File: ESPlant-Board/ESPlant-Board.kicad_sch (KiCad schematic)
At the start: 38 parts, among them J1 Conn_01x05, U1 HC-TYPE-C-16P-01A-G, U13 ESP32-C6-MINI-1/U, U3 AHT20-F, U4 Button, U6 Light sensor, U7 AMS1117-3_3, U8 MK-12C02-G025

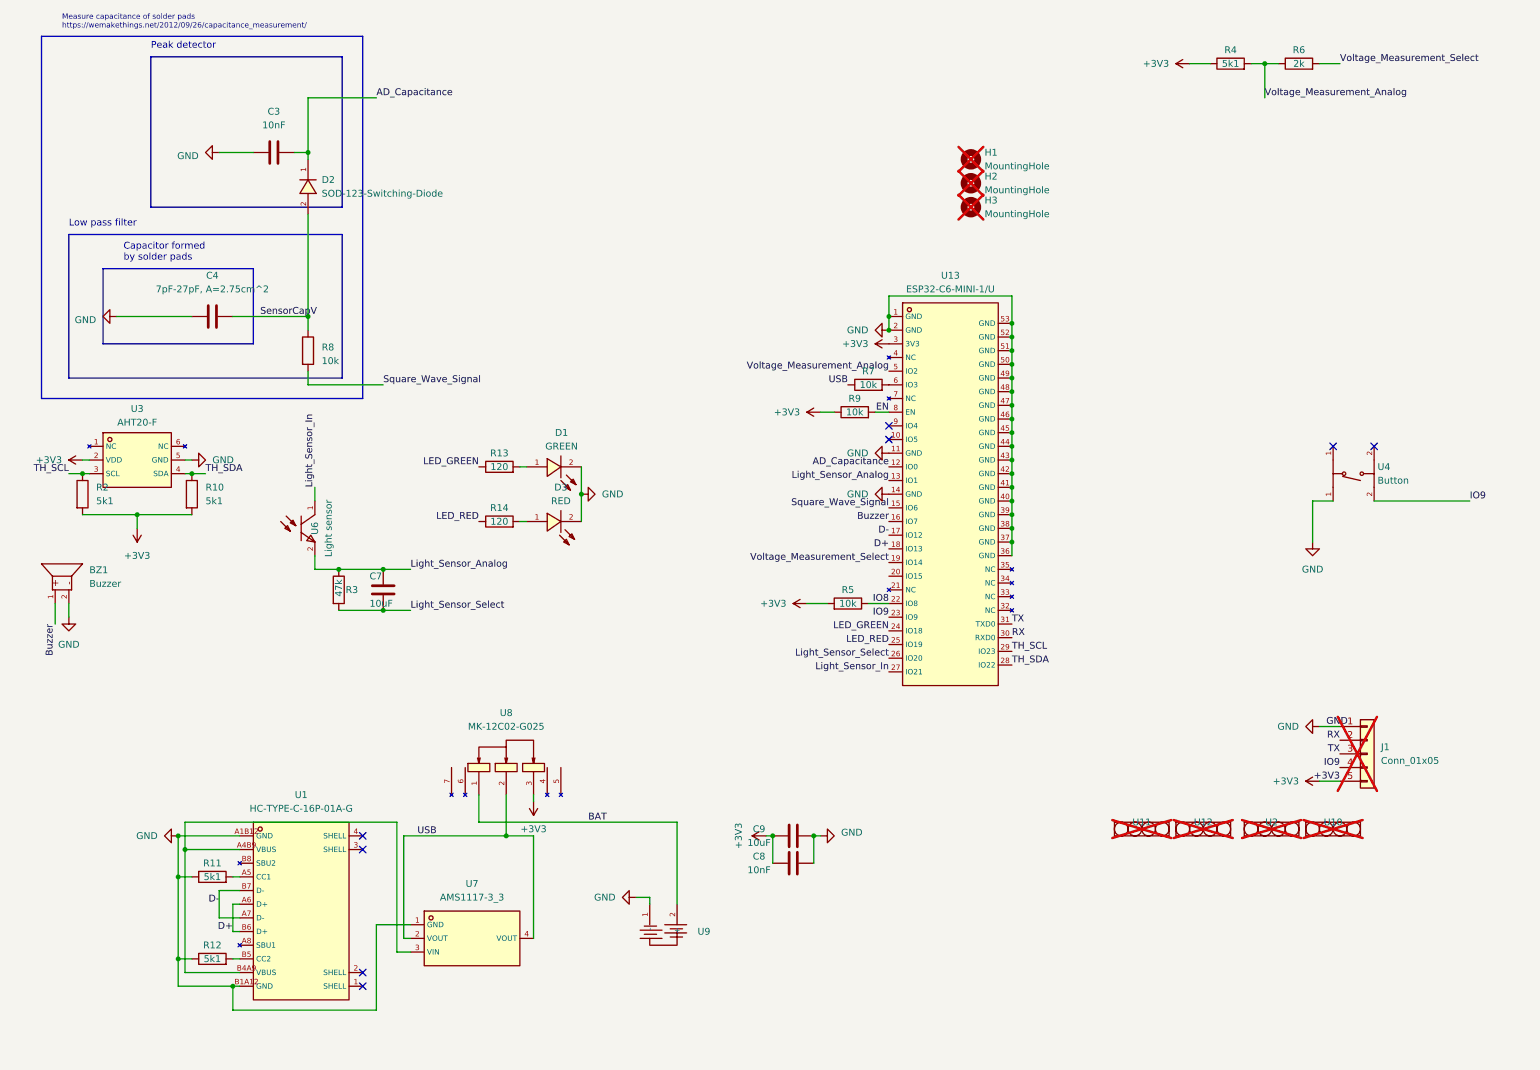
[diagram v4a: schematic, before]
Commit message: Board: New power supply chip
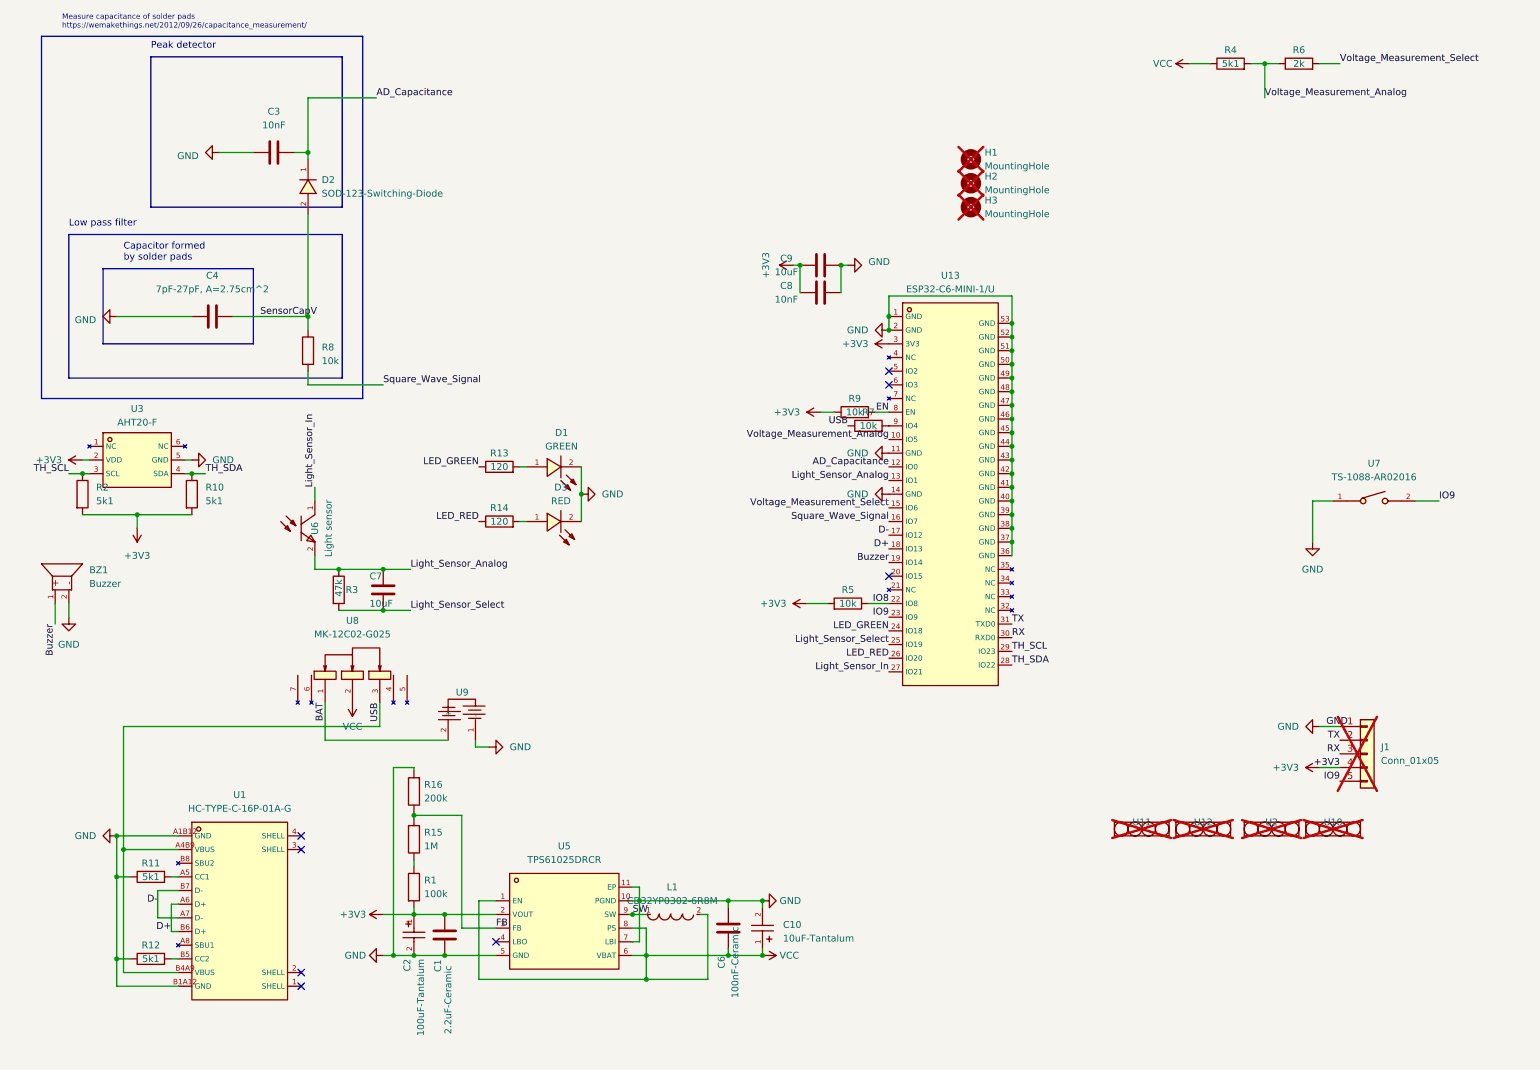
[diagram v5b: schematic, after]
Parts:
- removed U4: Button, CustomFootprints:SW-SMD_4P-L5.1-W5.1-P3.70-LS6.5-TL-2, symbol Custom_Parts:Button
- removed U7: AMS1117-3_3, CustomFootprints:SOT-223-3_L6.5-W3.4-P2.30-LS7.0-BR, symbol Custom_Parts:AMS1117_Voltage_Regulator
- added C1: 2.2uF-Ceramic, Capacitor_SMD:C_0402_1005Metric, symbol Device:C
- added C10: 10uF-Tantalum, CustomFootprints:CAP-SMD_L3.2-W1.6-RD-C7171, symbol Custom_Parts:TAJA106K016RNJ
- added C2: 100uF-Tantalum, CustomFootprints:CASE-B_3528, symbol Custom_Parts:TAJB107K006RNJ
- added C6: 100nF-Ceramic, Capacitor_SMD:C_0402_1005Metric, symbol Device:C
- added L1: CD32YP0302-6R8M, CustomFootprints:IND-SMD_L3.5-W3.0, symbol Custom_Parts:CD32YP0302-6R8M
- added R1: 100k, Resistor_SMD:R_0402_1005Metric, symbol Device:R
- added R15: 1M, Resistor_SMD:R_0402_1005Metric, symbol Device:R
- added R16: 200k, Resistor_SMD:R_0402_1005Metric, symbol Device:R
- added U5: TPS61025DRCR, CustomFootprints:VSON-10_L3.0-W3.0-P0.50-BL-EP_TPS62410DRCR, symbol Custom_Parts:TPS61025DRCR
- added U7: TS-1088-AR02016, CustomFootprints:SW-SMD_L3.9-W3.0-P4.45, symbol Custom_Parts:TS-1088-AR02016
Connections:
- net +3V3: now also J1.4 (Pin_4), C1.2, C2.1, R1.2, U5.2 (VOUT); no longer J1.5 (Pin_5), R4.1, U8.3
- net Buzzer: now also U13.19 (IO14); no longer U13.16 (IO7)
- net GND: now also C1.1, C10.2, C2.2, C6.2, R16.2, U5.10 (PGND), U5.11 (EP), U5.5 (GND), U5.7 (LBI), U7.1
- net IO9: now also J1.5 (Pin_5), U7.2; no longer J1.4 (Pin_4)
- net LED_RED: now also U13.26 (IO20); no longer U13.25 (IO19)
- net Light_Sensor_Select: now also U13.25 (IO19); no longer U13.26 (IO20)
- net RX: now also J1.3 (Pin_3); no longer J1.2 (Pin_2)
- net Square_Wave_Signal: now also U13.16 (IO7); no longer U13.15 (IO6)
- net TX: now also J1.2 (Pin_2); no longer J1.3 (Pin_3)
- net USB: now also U1.A4B9 (VBUS), U1.B4A9 (VBUS), U8.3; no longer U8.2
- net Voltage_Measurement_Analog: now also U13.10 (IO5); no longer U13.5 (IO2)
- net Voltage_Measurement_Select: now also U13.15 (IO6); no longer U13.19 (IO14)
- net at U13.6 (IO3): no longer R7.2
- net at U13.9 (IO4): now also R7.2
- new net: R1.1, R15.1
- new net FB: R15.2, R16.1, U5.3 (FB)
- new net SW: L1.1, U5.9 (SW)
- new net VCC: C10.1, C6.1, L1.2, R4.1, U5.1 (EN), U5.6 (VBAT), U5.8 (PS), U8.2
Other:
- moved on the sheet: C8, C9, R11, R12, R7, U1, U8, U9

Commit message: Update 100nF Capacitor
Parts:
- C6: LCSC C15195 -> C1525; MPN C15195 -> C1525
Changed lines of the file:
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@@
       (effects (font (size 1.27 1.27)) hide)
     )
-    (property "LCSC" "C15195" (at 142.875 178.435 0)
+    (property "LCSC" "C1525" (at 142.875 178.435 0)
       (effects (font (size 1.27 1.27)) hide)
     )
-    (property "MPN" "C15195" (at 142.875 178.435 0)
+    (property "MPN" "C1525" (at 142.875 178.435 0)
       (effects (font (size 1.27 1.27)) hide)
     )

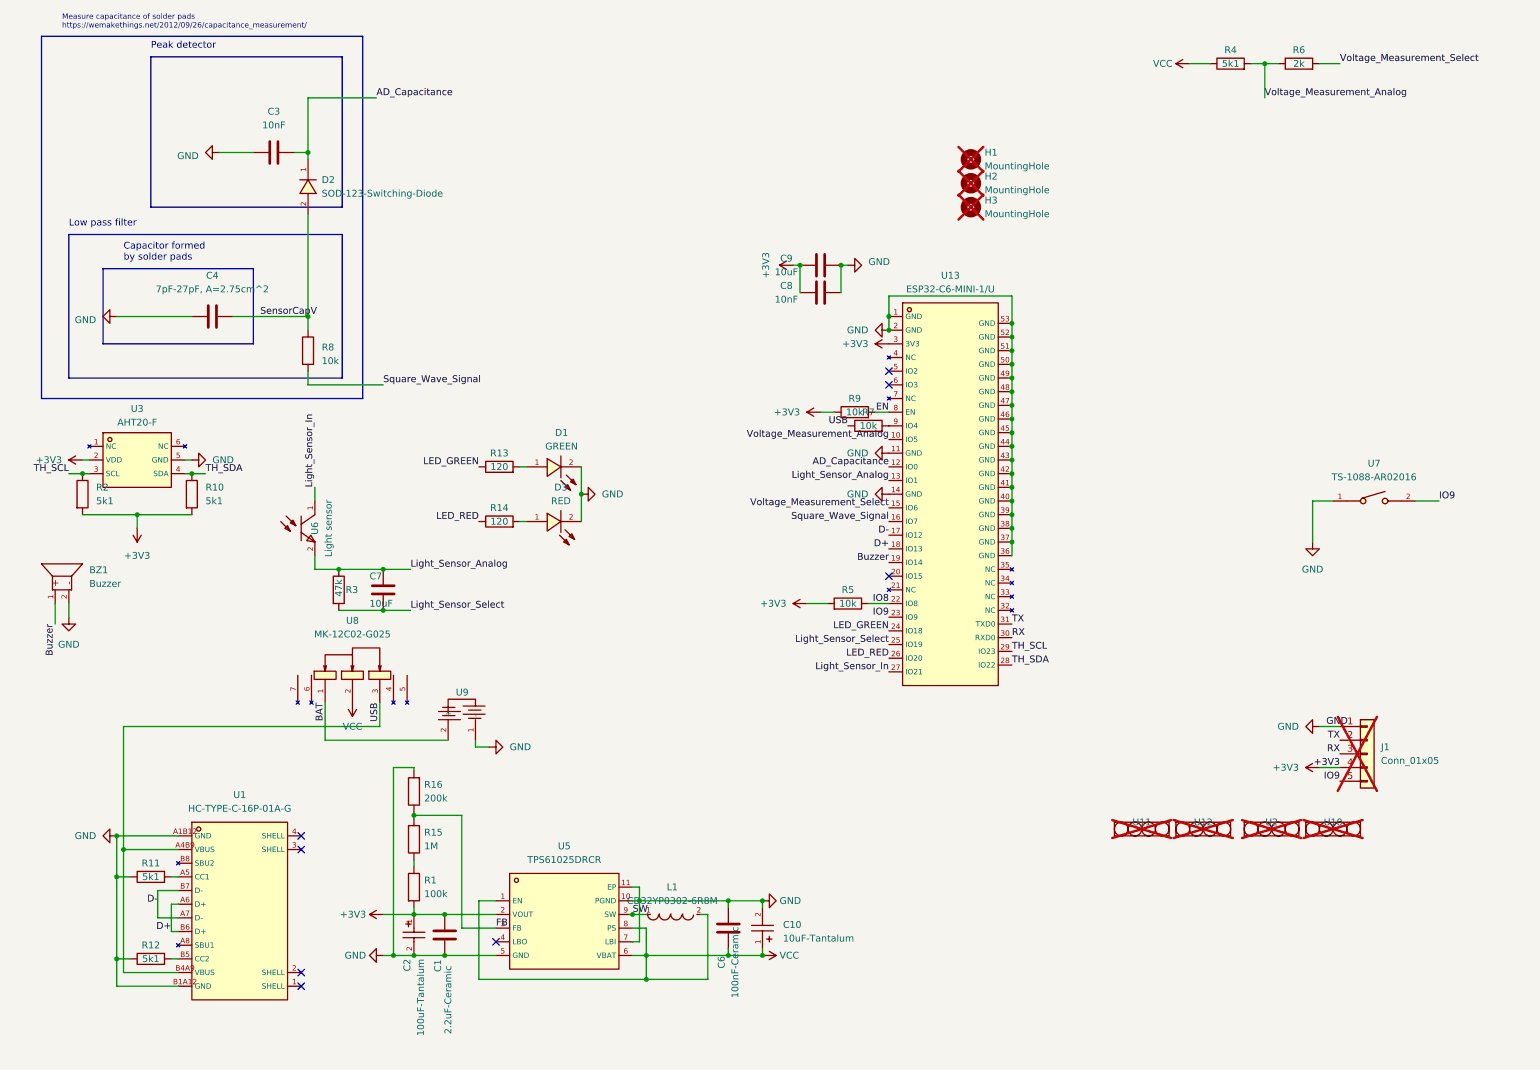
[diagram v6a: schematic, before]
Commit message: Board: Update Layout
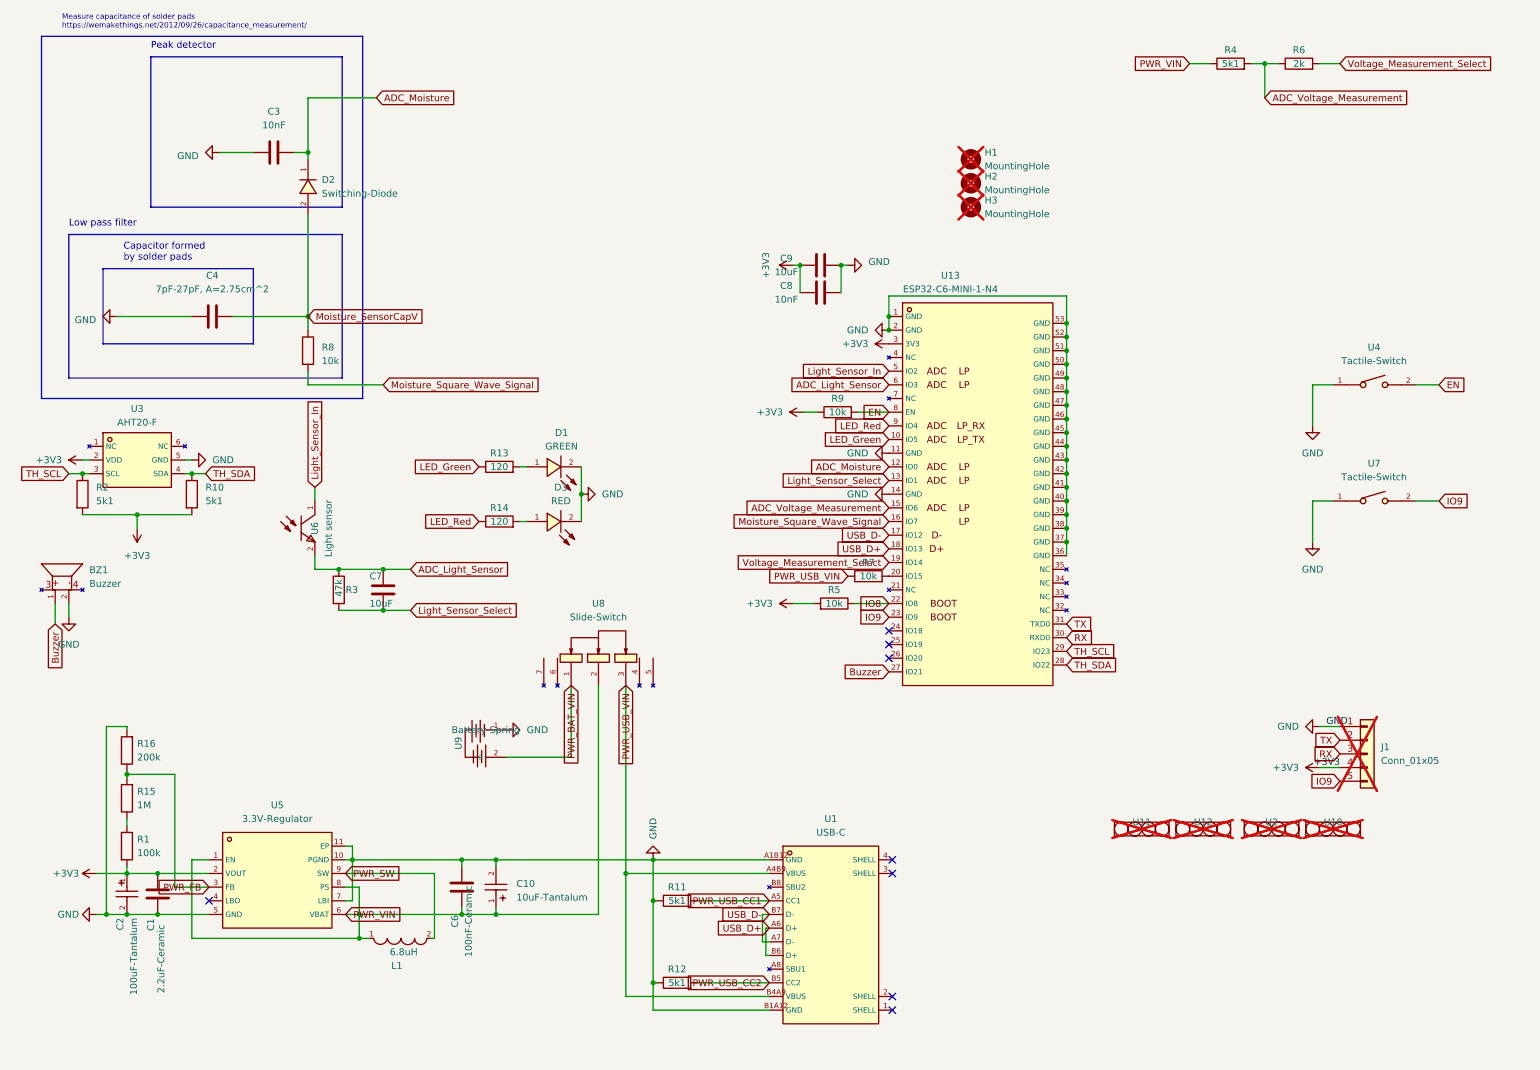
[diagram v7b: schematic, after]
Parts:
- added U4: Tactile-Switch, CustomFootprints:SW-SMD_L3.9-W3.0-P4.45, symbol Custom_Parts:TS-1088-AR02016
- D2: value SOD-123-Switching-Diode -> Switching-Diode
- L1: value CD32YP0302-6R8M -> 6.8uH
- U1: value HC-TYPE-C-16P-01A-G -> USB-C
- U13: value ESP32-C6-MINI-1/U -> ESP32-C6-MINI-1-N4
- U5: value TPS61025DRCR -> 3.3V-Regulator
- U7: value TS-1088-AR02016 -> Tactile-Switch
- U8: value MK-12C02-G025 -> Slide-Switch
- U9: value ~ -> Battery-Spring
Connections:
- net Buzzer: now also U13.27 (IO21); no longer U13.19 (IO14)
- net EN: now also U4.2
- net GND: now also U4.1
- net Light_Sensor_In: now also U13.5 (IO2); no longer U13.27 (IO21)
- net Light_Sensor_Select: now also U13.13 (IO1); no longer U13.25 (IO19)
- net Voltage_Measurement_Select: now also U13.19 (IO14); no longer U13.15 (IO6)
- net PWR_USB_CC2: now reaches R12.2, U1.B5 (CC2)
- net PWR_USB_CC1: now reaches R11.2, U1.A5 (CC1)
- net at U13.20 (IO15): now also R7.2
- net ADC_Light_Sensor: now reaches U13.6 (IO3)
- net ADC_Light_Sensor: now also C7.1, R3.1, U6.2 (E)
- net LED_Red: now reaches U13.9 (IO4)
- net LED_Red: now also R14.1; no longer R7.2
- net AD_Capacitance renamed ADC_Moisture
- net BAT renamed PWR_BAT_VIN
- net D+ renamed USB_D+
- net D- renamed USB_D-
- net FB renamed PWR_FB
- net LED_GREEN: no longer names the net of U13.24 (IO18)
- net LED_GREEN: no longer R13.1
- net LED_RED: no longer names the net of U13.26 (IO20)
- net LED_RED: no longer R14.1
- removed net Light_Sensor_Analog: C7.1, R3.1, U13.13 (IO1), U6.2 (E)
- net SW renamed PWR_SW
- net PWR_SW: now also L1.2; no longer L1.1
- net SensorCapV renamed Moisture_SensorCapV
- net Square_Wave_Signal renamed Moisture_Square_Wave_Signal
- net USB renamed PWR_USB_VIN
- net VCC renamed PWR_VIN
- net PWR_VIN: now also L1.1; no longer L1.2
- net Voltage_Measurement_Analog renamed ADC_Voltage_Measurement
- net ADC_Voltage_Measurement: now also U13.15 (IO6); no longer U13.10 (IO5)
- new net LED_Green: R13.1, U13.10 (IO5)
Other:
- moved on the sheet: C1, C10, C2, C6, L1, R1, R11, R12, R15, R16, R5, R7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
